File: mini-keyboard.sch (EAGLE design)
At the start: 28 parts, among them P1 500, P2 500, P3 500, P4 500, P5 500, P6 500, P7 500, P8 500, U1 SN74HC148DIP, U2 CD4512BE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

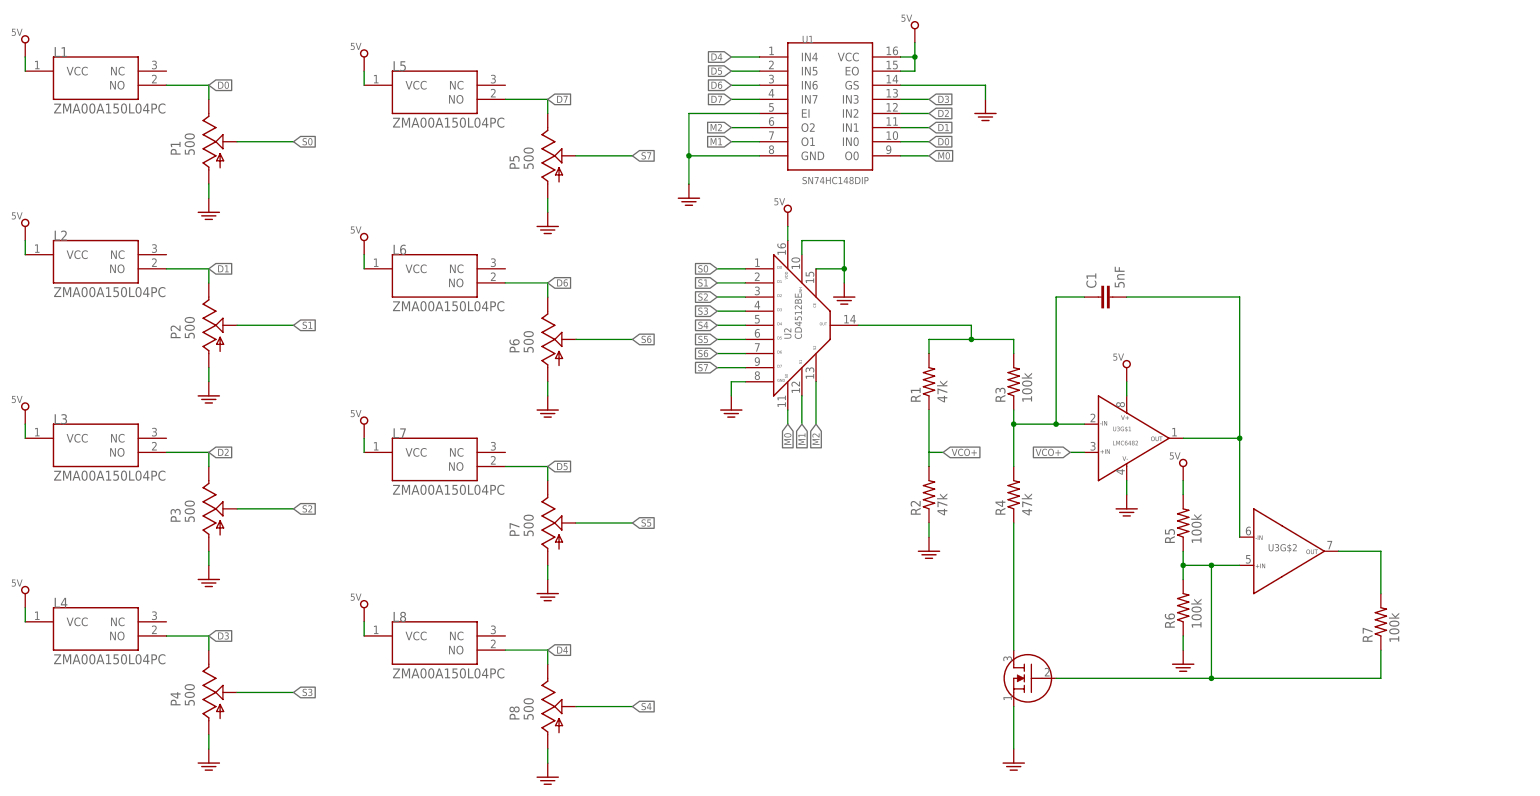
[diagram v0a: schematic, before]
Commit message: Finished board, added pwr connector, LED, and audio connector for 3.5mm stereo
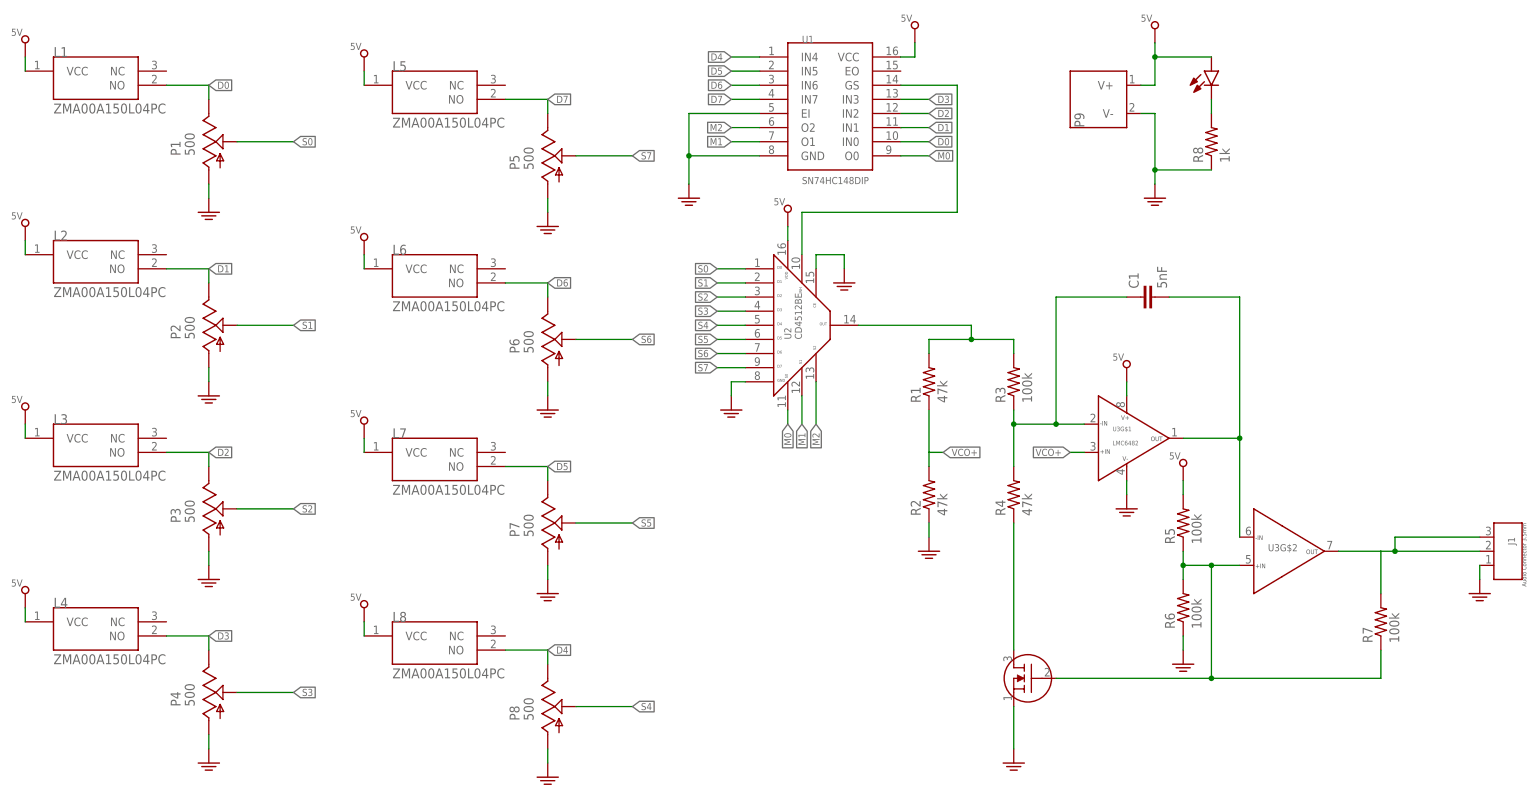
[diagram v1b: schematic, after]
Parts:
- added J1: SJ-3523-SMT, audio-connectors:SJ-3523-SMT
- added P9: (no value), PWR-Connectors:SINGLE-LINE
- added PWR: LED-STD, LED:LED-STD
- added R8: 1k, RCL:R0603
- renumbered U$23 to U23
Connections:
- new net N$3: U1.GS, U2.INHIBIT
- new net N$7: PWR.OUT, R8.P$2
- net 5V: now also P9.V+, PWR.IN; no longer U1.EO
- net GND: now also J1.1, P9.V-, R8.P$1; no longer U1.GS, U2.INHIBIT
- net N$5: now also J1.2, J1.3
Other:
- moved on the sheet: C1
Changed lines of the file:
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@@
 <setting verticaltext="up"/>
 </settings>
-<grid distance="0.1" unitdist="inch" unit="inch" style="lines" multiple="1" display="yes" altdistance="0.01" altunitdist="inch" altunit="inch"/>
+<grid distance="0.1" unitdist="inch" unit="inch" style="lines" multiple="1" display="no" altdistance="0.01" altunitdist="inch" altunit="inch"/>
 <layers>
 <layer number="1" name="Top" color="4" fill="1" visible="no" active="no"/>
@@
 <part name="U$18" library="pwr_gnd" deviceset="5V" device=""/>
 <part name="U$19" library="pwr_gnd" deviceset="GND" device=""/>
-<part name="U$17" library="pwr_gnd" deviceset="GND" device=""/>
 <part name="U2" library="logic" deviceset="CD4512" device="BE"/>
 <part name="U$20" library="pwr_gnd" deviceset="5V" device=""/>
 <part name="U$21" library="pwr_gnd" deviceset="GND" device=""/>
-<part name="U$22" library="pwr_gnd" deviceset="GND" device=""/>
 <part name="R1" library="RCL" deviceset="R" device="0603" value="47k"/>
 <part name="R2" library="RCL" deviceset="R" device="0603" value="47k"/>
@@
 <part name="U$28" library="pwr_gnd" deviceset="5V" device=""/>
 <part name="U$29" library="pwr_gnd" deviceset="GND" device=""/>
-<part name="U$23" library="Transistors" deviceset="2N7000" device="-G"/>
+<part name="U23" library="Transistors" deviceset="2N7000" device="-G"/>
+<part name="U$17" library="pwr_gnd" deviceset="GND" device=""/>
+<part name="P9" library="PWR-Connectors" deviceset="SINGLE-LINE" device=""/>
+<part name="U$22" library="pwr_gnd" deviceset="5V" device=""/>
+<part name="U$30" library="pwr_gnd" deviceset="GND" device=""/>
+<part name="J1" library="audio-connectors" deviceset="SJ-3523-SMT" device=""/>
+<part name="U$23" library="pwr_gnd" deviceset="GND" device=""/>
+<part name="PWR" library="LED" deviceset="LED-STD" device=""/>
+<part name="R8" library="RCL" deviceset="R" device="0603" value="1k"/>
 </parts>
 <sheets>
@@
 <instance part="U$18" gate="G$1" x="132.08" y="17.78"/>
 <instance part="U$19" gate="G$1" x="91.44" y="-12.7"/>
-<instance part="U$17" gate="G$1" x="144.78" y="2.54"/>
 <instance part="U2" gate="G$1" x="109.22" y="-35.56"/>
 <instance part="U$20" gate="G$1" x="109.22" y="-15.24"/>
 <instance part="U$21" gate="G$1" x="99.06" y="-50.8"/>
-<instance part="U$22" gate="G$1" x="119.38" y="-30.48"/>
 <instance part="R1" gate="G$1" x="134.62" y="-45.72" rot="R90"/>
 <instance part="R2" gate="G$1" x="134.62" y="-66.04" rot="R90"/>
@@
 <instance part="R6" gate="G$1" x="180.34" y="-86.36" rot="R90"/>
 <instance part="R7" gate="G$1" x="215.9" y="-88.9" rot="R90"/>
-<instance part="C1" gate="G$1" x="167.64" y="-30.48"/>
+<instance part="C1" gate="G$1" x="175.26" y="-30.48"/>
 <instance part="U3" gate="G$1" x="170.18" y="-55.88"/>
 <instance part="U3" gate="G$2" x="198.12" y="-76.2"/>
@@
 <instance part="U$28" gate="G$1" x="180.34" y="-60.96"/>
 <instance part="U$29" gate="G$1" x="170.18" y="-68.58"/>
-<instance part="U$23" gate="G$1" x="152.4" y="-99.06"/>
+<instance part="U23" gate="G$1" x="152.4" y="-99.06"/>
+<instance part="U$17" gate="G$1" x="119.38" y="-27.94"/>
+<instance part="P9" gate="G$1" x="165.1" y="5.08"/>
+<instance part="U$22" gate="G$1" x="175.26" y="17.78"/>
+<instance part="U$30" gate="G$1" x="175.26" y="-12.7"/>
+<instance part="J1" gate="G$1" x="238.76" y="-76.2" rot="R180"/>
+<instance part="U$23" gate="G$1" x="233.68" y="-83.82"/>
+<instance part="PWR" gate="G$1" x="185.42" y="7.62" rot="R270"/>
+<instance part="R8" gate="G$1" x="185.42" y="-2.54" rot="R90"/>
 </instances>
 <busses>
@@
 <wire x1="129.54" y1="12.7" x2="132.08" y2="12.7" width="0.1524" layer="91"/>
 <wire x1="132.08" y1="12.7" x2="132.08" y2="15.24" width="0.1524" layer="91"/>
-<pinref part="U1" gate="G$1" pin="EO"/>
-<wire x1="129.54" y1="10.16" x2="132.08" y2="10.16" width="0.1524" layer="91"/>
-<wire x1="132.08" y1="10.16" x2="132.08" y2="12.7" width="0.1524" layer="91"/>
-<junction x="132.08" y="12.7"/>
 </segment>
 <segment>
@@
 <pinref part="U3" gate="G$1" pin="VCC"/>
 <wire x1="170.18" y1="-45.72" x2="170.18" y2="-48.26" width="0.1524" layer="91"/>
+</segment>
+<segment>
+<pinref part="U$22" gate="G$1" pin="5V"/>
+<pinref part="P9" gate="G$1" pin="V+"/>
+<wire x1="175.26" y1="15.24" x2="175.26" y2="12.7" width="0.1524" layer="91"/>
+<wire x1="175.26" y1="12.7" x2="175.26" y2="7.62" width="0.1524" layer="91"/>
+<wire x1="175.26" y1="7.62" x2="172.72" y2="7.62" width="0.1524" layer="91"/>
+<pinref part="PWR" gate="G$1" pin="IN"/>
+<wire x1="175.26" y1="12.7" x2="185.42" y2="12.7" width="0.1524" layer="91"/>
+<junction x="175.26" y="12.7"/>
 </segment>
 </net>
@@
 </segment>
 <segment>
-<pinref part="U1" gate="G$1" pin="GS"/>
-<wire x1="129.54" y1="7.62" x2="144.78" y2="7.62" width="0.1524" layer="91"/>
-<wire x1="144.78" y1="7.62" x2="144.78" y2="5.08" width="0.1524" layer="91"/>
-<pinref part="U$17" gate="G$1" pin="GND"/>
-</segment>
-<segment>
 <pinref part="U2" gate="G$1" pin="GND"/>
 <wire x1="101.6" y1="-45.72" x2="99.06" y2="-45.72" width="0.1524" layer="91"/>
@@
 </segment>
 <segment>
-<pinref part="U2" gate="G$1" pin="INHIBIT"/>
-<wire x1="111.76" y1="-22.86" x2="111.76" y2="-20.32" width="0.1524" layer="91"/>
-<wire x1="111.76" y1="-20.32" x2="119.38" y2="-20.32" width="0.1524" layer="91"/>
-<wire x1="119.38" y1="-20.32" x2="119.38" y2="-25.4" width="0.1524" layer="91"/>
-<pinref part="U2" gate="G$1" pin="DISABLE"/>
-<wire x1="119.38" y1="-25.4" x2="119.38" y2="-27.94" width="0.1524" layer="91"/>
-<wire x1="114.3" y1="-25.4" x2="119.38" y2="-25.4" width="0.1524" layer="91"/>
-<junction x="119.38" y="-25.4"/>
-<pinref part="U$22" gate="G$1" pin="GND"/>
-</segment>
-<segment>
 <pinref part="R6" gate="G$1" pin="P$1"/>
 <pinref part="U$26" gate="G$1" pin="GND"/>
@@
 </segment>
 <segment>
-<pinref part="U$23" gate="G$1" pin="S"/>
+<pinref part="U23" gate="G$1" pin="S"/>
 <pinref part="U$27" gate="G$1" pin="GND"/>
 <wire x1="149.86" y1="-111.76" x2="149.86" y2="-104.14" width="0.1524" layer="91"/>
+</segment>
+<segment>
+<pinref part="U2" gate="G$1" pin="DISABLE"/>
+<wire x1="114.3" y1="-25.4" x2="114.3" y2="-22.86" width="0.1524" layer="91"/>
+<wire x1="114.3" y1="-22.86" x2="119.38" y2="-22.86" width="0.1524" layer="91"/>
+<pinref part="U$17" gate="G$1" pin="GND"/>
+<wire x1="119.38" y1="-22.86" x2="119.38" y2="-25.4" width="0.1524" layer="91"/>
+</segment>
+<segment>
+<pinref part="P9" gate="G$1" pin="V-"/>
+<pinref part="U$30" gate="G$1" pin="GND"/>
+<wire x1="172.72" y1="2.54" x2="175.26" y2="2.54" width="0.1524" layer="91"/>
+<wire x1="175.26" y1="2.54" x2="175.26" y2="-7.62" width="0.1524" layer="91"/>
+<pinref part="R8" gate="G$1" pin="P$1"/>
+<wire x1="175.26" y1="-7.62" x2="175.26" y2="-10.16" width="0.1524" layer="91"/>
+<wire x1="185.42" y1="-7.62" x2="175.26" y2="-7.62" width="0.1524" layer="91"/>
+<junction x="175.26" y="-7.62"/>
+</segment>
+<segment>
+<pinref part="J1" gate="G$1" pin="1"/>
+<pinref part="U$23" gate="G$1" pin="GND"/>
+<wire x1="233.68" y1="-78.74" x2="233.68" y2="-81.28" width="0.1524" layer="91"/>
 </segment>
 </net>
@@
 <wire x1="157.48" y1="-53.34" x2="157.48" y2="-30.48" width="0.1524" layer="91"/>
 <pinref part="C1" gate="G$1" pin="1"/>
-<wire x1="157.48" y1="-30.48" x2="162.56" y2="-30.48" width="0.1524" layer="91"/>
+<wire x1="157.48" y1="-30.48" x2="170.18" y2="-30.48" width="0.1524" layer="91"/>
 <junction x="157.48" y="-53.34"/>
 </segment>
@@
 <wire x1="208.28" y1="-76.2" x2="215.9" y2="-76.2" width="0.1524" layer="91"/>
 <wire x1="215.9" y1="-76.2" x2="215.9" y2="-83.82" width="0.1524" layer="91"/>
+<wire x1="215.9" y1="-76.2" x2="218.44" y2="-76.2" width="0.1524" layer="91"/>
+<wire x1="218.44" y1="-76.2" x2="218.44" y2="-73.66" width="0.1524" layer="91"/>
+<pinref part="J1" gate="G$1" pin="3"/>
+<wire x1="218.44" y1="-73.66" x2="233.68" y2="-73.66" width="0.1524" layer="91"/>
+<pinref part="J1" gate="G$1" pin="2"/>
+<wire x1="218.44" y1="-76.2" x2="233.68" y2="-76.2" width="0.1524" layer="91"/>
+<junction x="218.44" y="-76.2"/>
 </segment>
 </net>
@@
 <junction x="185.42" y="-78.74"/>
 <junction x="180.34" y="-78.74"/>
-<pinref part="U$23" gate="G$1" pin="G"/>
+<pinref part="U23" gate="G$1" pin="G"/>
 <wire x1="157.48" y1="-99.06" x2="185.42" y2="-99.06" width="0.1524" layer="91"/>
 <junction x="185.42" y="-99.06"/>
@@
 <wire x1="190.5" y1="-55.88" x2="180.34" y2="-55.88" width="0.1524" layer="91"/>
 <pinref part="C1" gate="G$1" pin="2"/>
-<wire x1="170.18" y1="-30.48" x2="190.5" y2="-30.48" width="0.1524" layer="91"/>
+<wire x1="177.8" y1="-30.48" x2="190.5" y2="-30.48" width="0.1524" layer="91"/>
 <wire x1="190.5" y1="-30.48" x2="190.5" y2="-55.88" width="0.1524" layer="91"/>
 <junction x="190.5" y="-55.88"/>
@@
 <segment>
 <pinref part="R4" gate="G$1" pin="P$1"/>
-<pinref part="U$23" gate="G$1" pin="D"/>
+<pinref part="U23" gate="G$1" pin="D"/>
 <wire x1="149.86" y1="-71.12" x2="149.86" y2="-93.98" width="0.1524" layer="91"/>
 </segment>
 </net>
+<net name="N$3" class="0">
+<segment>
+<pinref part="U1" gate="G$1" pin="GS"/>
+<wire x1="129.54" y1="7.62" x2="139.7" y2="7.62" width="0.1524" layer="91"/>
+<wire x1="139.7" y1="7.62" x2="139.7" y2="-15.24" width="0.1524" layer="91"/>
+<pinref part="U2" gate="G$1" pin="INHIBIT"/>
+<wire x1="139.7" y1="-15.24" x2="111.76" y2="-15.24" width="0.1524" layer="91"/>
+<wire x1="111.76" y1="-15.24" x2="111.76" y2="-22.86" width="0.1524" layer="91"/>
+</segment>
+</net>
+<net name="N$7" class="0">
+<segment>
+<pinref part="PWR" gate="G$1" pin="OUT"/>
+<pinref part="R8" gate="G$1" pin="P$2"/>
+<wire x1="185.42" y1="5.08" x2="185.42" y2="2.54" width="0.1524" layer="91"/>
+</segment>
+</net>
